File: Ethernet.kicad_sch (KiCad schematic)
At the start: 34 parts, among them J12 7499010211A, U12 LAN8742A, U13 USBLC6-4SC6, Y3 25Mhz

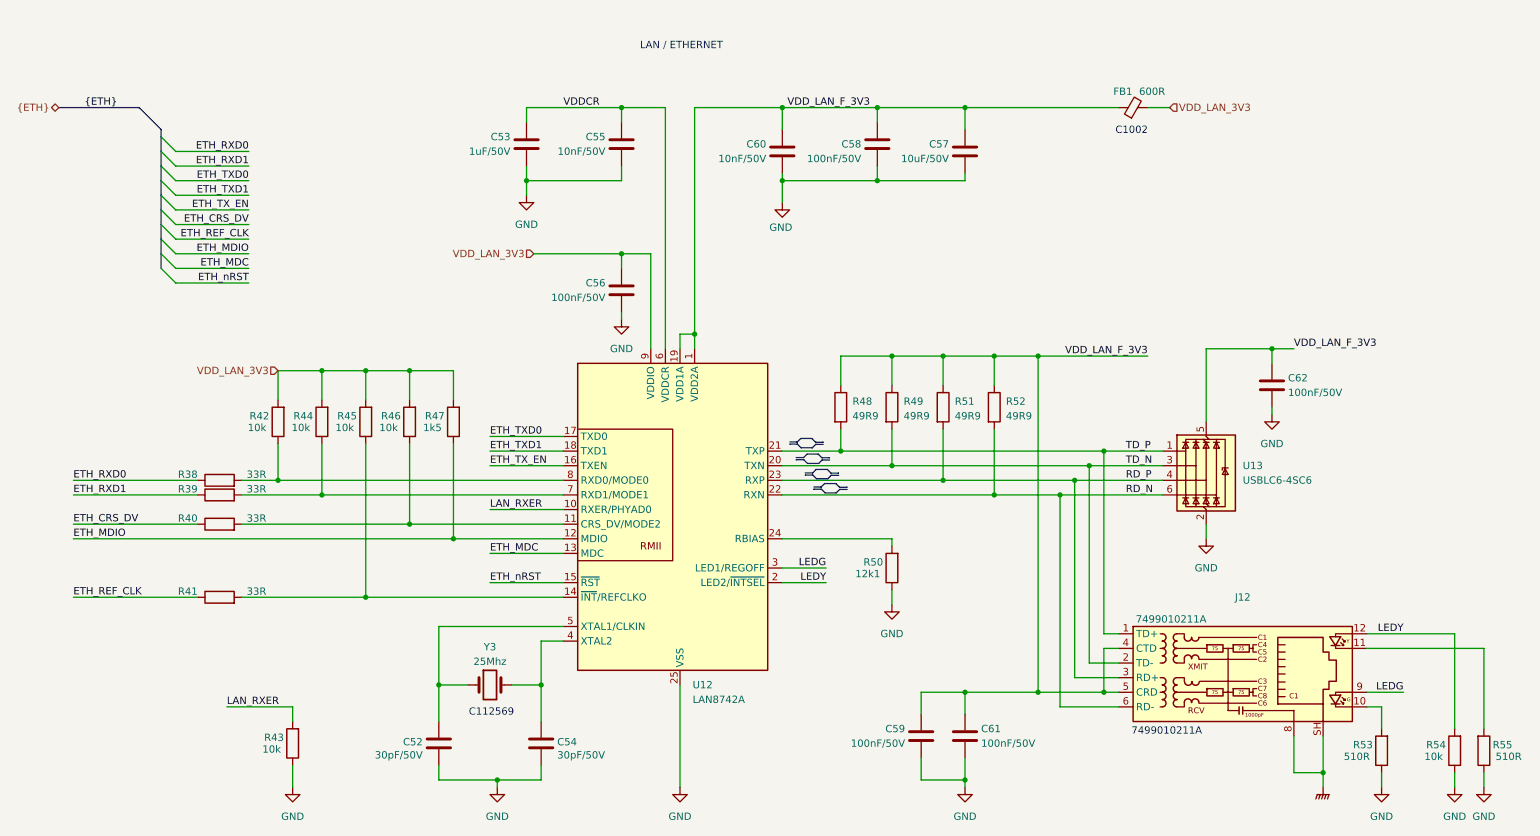
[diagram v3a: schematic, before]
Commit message: Se empieza a evaluar la conexión del ethernet con la carcasa, parte analog, dig y micro en posición, tambien se busca solución para la salida de led de las entradas digitales
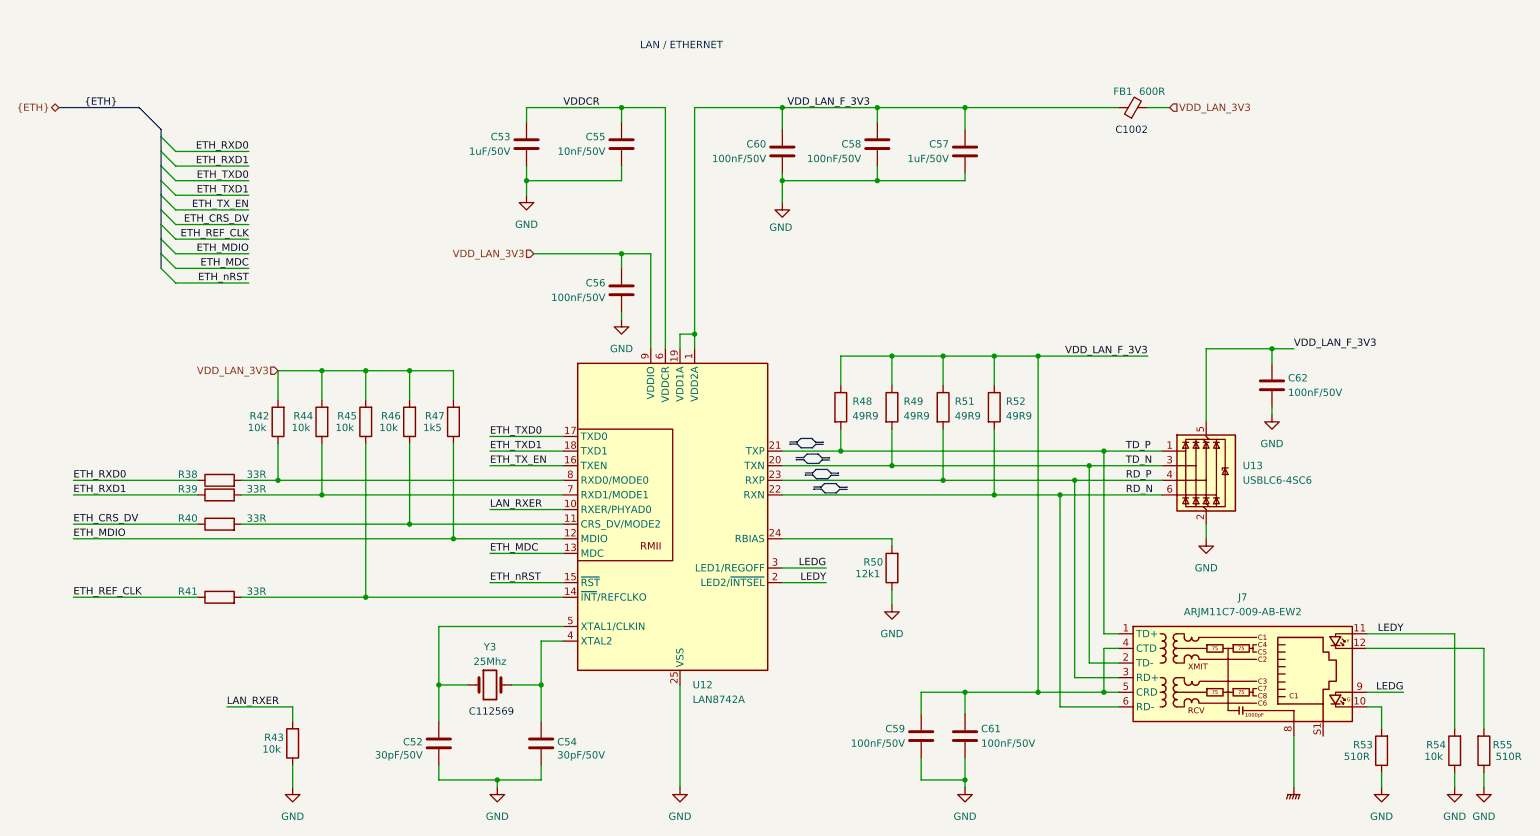
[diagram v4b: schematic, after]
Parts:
- removed J12: 7499010211A, Connector_RJ:RJ45_Wuerth_7499010211A_Horizontal, symbol Connector:RJ45_Wuerth_7499010211A
- added J7: ARJM11C7-009-AB-EW2, LIB_PCB_CONT:ARJM11C7-009-AB-EW2_Abracon, symbol LIB_SCH_CONTR:ARJM11C7-009-AB-EW2
- C57: value 10uF/50V -> 1uF/50V
- C60: value 10nF/50V -> 100nF/50V
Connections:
- net GNDPWR: now also J7.8
- net LEDG: now also J7.9
- net LEDY: now also J7.11
- net RD_N: now also J7.6 (RD-)
- net RD_P: now also J7.3 (RD+)
- net TD_N: now also J7.2 (TD-)
- net TD_P: now also J7.1 (TD+)
- net VDD_LAN_F_3V3: now also J7.4 (CTD), J7.5 (CRD)
- net at R53.2: now also J7.10
- net at R55.2: now also J7.12
- new net: J7.S1, J7.S2
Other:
- note removed: "7499010211A"
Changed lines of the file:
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@@
 		)
 	)
-	(text "7499010211A"
-		(exclude_from_sim no)
-		(at 221.742 140.208 0)
-		(effects
-			(font
-				(size 1.27 1.27)
-			)
-		)
-	)
 	(text "C1002"
 		(exclude_from_sim no)
@@
 	)
 	(junction
-		(at 248.92 147.32)
-		(diameter 0)
-		(color 0 0 0 0)
-	)
-	(junction
 		(at 97.79 106.68)
 		(diameter 0)
@@
 	(wire
 		(pts
-			(xy 248.92 140.97) (xy 248.92 147.32)
-		)
-		(stroke
-			(width 0)
-			(type default)
-		)
-	)
-	(wire
-		(pts
 			(xy 228.6 104.14) (xy 228.6 106.68)
 		)
@@
 		)
 	)
-	(wire
-		(pts
-			(xy 243.84 147.32) (xy 248.92 147.32)
-		)
-		(stroke
-			(width 0)
-			(type default)
-		)
-	)
 	(polyline
 		(pts
@@
 	(wire
 		(pts
-			(xy 248.92 147.32) (xy 248.92 149.86)
+			(xy 243.84 140.97) (xy 243.84 149.86)
 		)
 		(stroke
@@
 	(wire
 		(pts
-			(xy 243.84 140.97) (xy 243.84 147.32)
-		)
-		(stroke
-			(width 0)
-			(type default)
-		)
-	)
-	(wire
-		(pts
 			(xy 67.31 90.17) (xy 67.31 96.52)
 		)
@@
 			)
 		)
-		(property "Value" "10uF/50V"
+		(property "Value" "1uF/50V"
 			(at 183.896 40.64 0)
 			(effects
@@
 	(symbol
 		(lib_id "power:GNDPWR")
-		(at 248.92 149.86 0)
+		(at 243.84 149.86 0)
 		(unit 1)
 		(exclude_from_sim no)
@@
 		(dnp no)
 		(property "Reference" "#PWR051"
-			(at 248.92 154.94 0)
+			(at 243.84 154.94 0)
 			(effects
 				(font
@@
 		)
 		(property "Value" "GNDPWR"
-			(at 246.634 154.178 0)
+			(at 241.554 154.178 0)
 			(effects
 				(font
@@
 		)
 		(property "Footprint" ""
-			(at 248.92 151.13 0)
+			(at 243.84 151.13 0)
 			(effects
 				(font
@@
 		)
 		(property "Datasheet" ""
-			(at 248.92 151.13 0)
+			(at 243.84 151.13 0)
 			(effects
 				(font
@@
 		)
 		(property "Description" "Power symbol creates a global label with name \"GNDPWR\" , global ground"
-			(at 248.92 149.86 0)
+			(at 243.84 149.86 0)
 			(effects
 				(font
@@
 	)
 	(symbol
-		(lib_id "Connector:RJ45_Wuerth_7499010211A")
+		(lib_id "LIB_SCH_CONTR:ARJM11C7-009-AB-EW2")
 		(at 233.68 130.81 0)
 		(unit 1)
@@
 		(on_board yes)
 		(dnp no)
-		(property "Reference" "J12"
+		(fields_autoplaced yes)
+		(property "Reference" "J7"
 			(at 234.95 116.84 0)
 			(effects
@@
 			)
 		)
-		(property "Value" "7499010211A"
-			(at 222.504 120.65 0)
+		(property "Value" "ARJM11C7-009-AB-EW2"
+			(at 234.95 119.38 0)
 			(effects
 				(font
@@
 			)
 		)
-		(property "Footprint" "Connector_RJ:RJ45_Wuerth_7499010211A_Horizontal"
+		(property "Footprint" "LIB_PCB_CONT:ARJM11C7-009-AB-EW2_Abracon"
 			(at 233.68 118.11 0)
 			(effects
@@
 			)
 		)
-		(property "Datasheet" "https://www.we-online.com/components/products/datasheet/7499010211A.pdf"
+		(property "Datasheet" "https://abracon.com/Magnetics/ARJM11.pdf"
 			(at 233.68 114.3 0)
 			(effects
@@
 			)
 		)
-		(pin "12"
+		(pin "1"
 		)
-		(pin "7"
+		(pin "2"
 		)
-		(pin "SH"
+		(pin "11"
 		)
-		(pin "9"
+		(pin "S2"
 		)
-		(pin "3"
+		(pin "5"
 		)
-		(pin "10"
+		(pin "4"
 		)
-		(pin "2"
+		(pin "9"
 		)
-		(pin "1"
+		(pin "10"
 		)
 		(pin "8"
 		)
-		(pin "5"
-		)
-		(pin "11"
+		(pin "S1"
 		)
 		(pin "6"
 		)
-		(pin "4"
+		(pin "3"
+		)
+		(pin "7"
+		)
+		(pin "12"
 		)
 		(instances
 			(project ""
-				(path "/7cf65f8a-f9e1-4c97-ae3b-2bf5316c4d48/15cecee3-3ea4-4fda-9934-a7d023f81ee7"
-					(reference "J4")
-					(unit 1)
-				)
-			)
-			(project ""
 				(path "/af529cf8-e3d6-4568-89be-bc7010f8b835/8e0b582f-0020-4bc2-aca5-707ed1850aed"
-					(reference "J12")
+					(reference "J7")
 					(unit 1)
 				)
@@
 			)
 		)
-		(property "Value" "10nF/50V"
+		(property "Value" "100nF/50V"
 			(at 152.146 40.64 0)
 			(effects

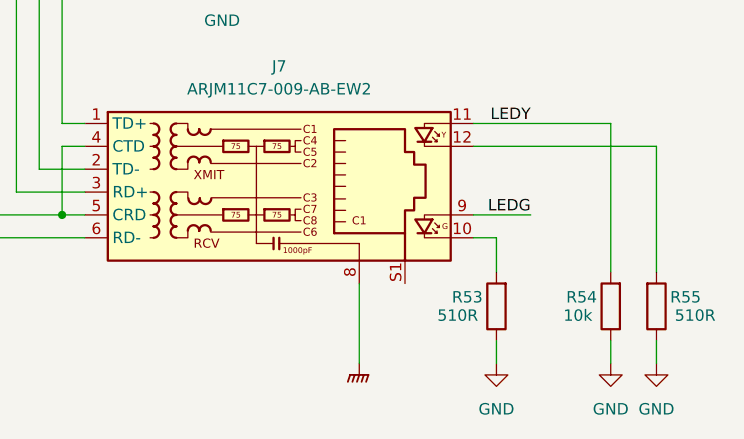
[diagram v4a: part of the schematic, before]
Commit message: Se traza vcc, digital, analog, relay, esta por terminar corregir GND y revisar nuevamente
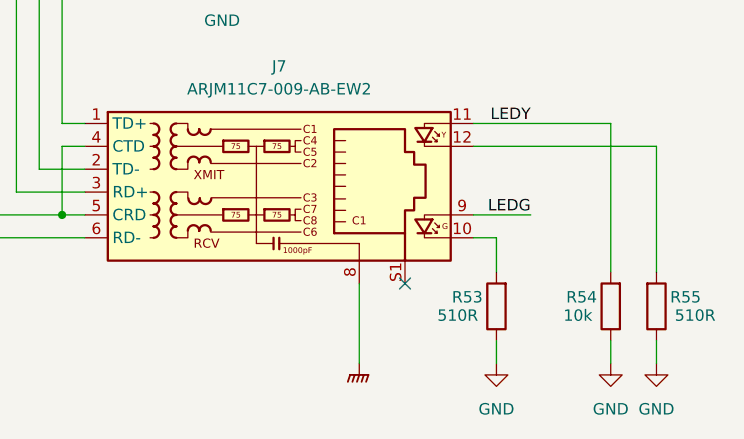
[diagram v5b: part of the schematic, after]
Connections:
- no-connect marks 0 -> 1
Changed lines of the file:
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@@
 		(color 0 0 0 0)
+	)
+	(no_connect
+		(at 248.92 140.97)
 	)
 	(bus_entry

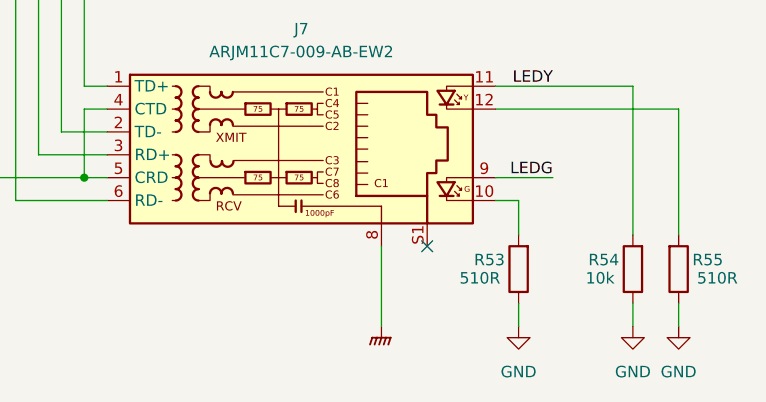
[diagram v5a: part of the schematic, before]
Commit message: Se termina de revisar la placa. Se corrige la terminación de los transformadores internos del puerto ethernet. Se revisa GND, espaciado, añadimos notas. Falta enlazar las partes de JLCPCN
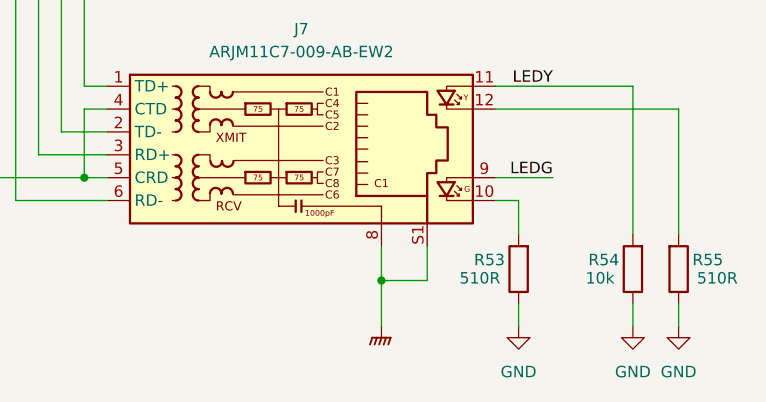
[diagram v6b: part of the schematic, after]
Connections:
- net GNDPWR: now also J7.S1, J7.S2
- no-connect marks 1 -> 0
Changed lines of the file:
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@@
+	)
+	(junction
+		(at 243.84 144.78)
+		(diameter 0)
+		(color 0 0 0 0)
 	)
 	(junction
@@
 		(color 0 0 0 0)
 	)
-	(no_connect
-		(at 248.92 140.97)
-	)
 	(bus_entry
 		(at 46.99 44.45)
@@
 	(wire
 		(pts
+			(xy 243.84 144.78) (xy 243.84 149.86)
+		)
+		(stroke
+			(width 0)
+			(type default)
+		)
+	)
+	(wire
+		(pts
 			(xy 154.94 44.45) (xy 154.94 48.26)
 		)
@@
 		)
 	)
+	(wire
+		(pts
+			(xy 248.92 140.97) (xy 248.92 144.78)
+		)
+		(stroke
+			(width 0)
+			(type default)
+		)
+	)
 	(polyline
 		(pts
@@
 	(wire
 		(pts
+			(xy 248.92 144.78) (xy 243.84 144.78)
+		)
+		(stroke
+			(width 0)
+			(type default)
+		)
+	)
+	(wire
+		(pts
 			(xy 137.16 71.12) (xy 137.16 73.66)
 		)
@@
 	(wire
 		(pts
-			(xy 243.84 140.97) (xy 243.84 149.86)
-		)
-		(stroke
+			(xy 243.84 140.97) (xy 243.84 144.78)
+		)
+		(stroke

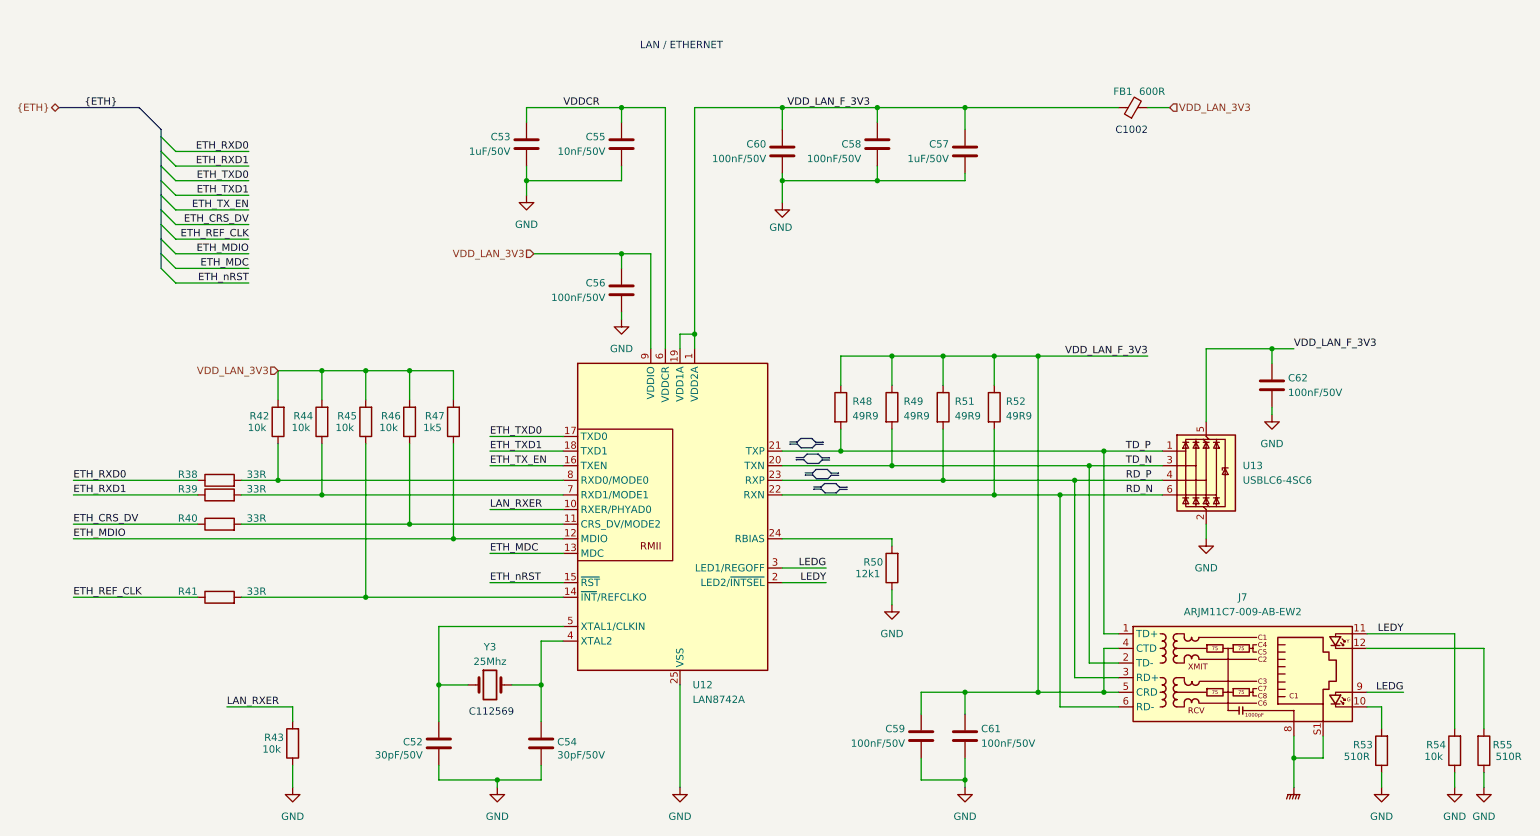
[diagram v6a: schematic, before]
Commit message: Se añaden leds a la entrada de los Namur. Se estandariza y revisan varios footprints de los capacitores. El cambio no fue demasiado, se corrigio en placa. Se hacen algunos cambios adicionales a los valores. Se realiza un avance para jlcpcb
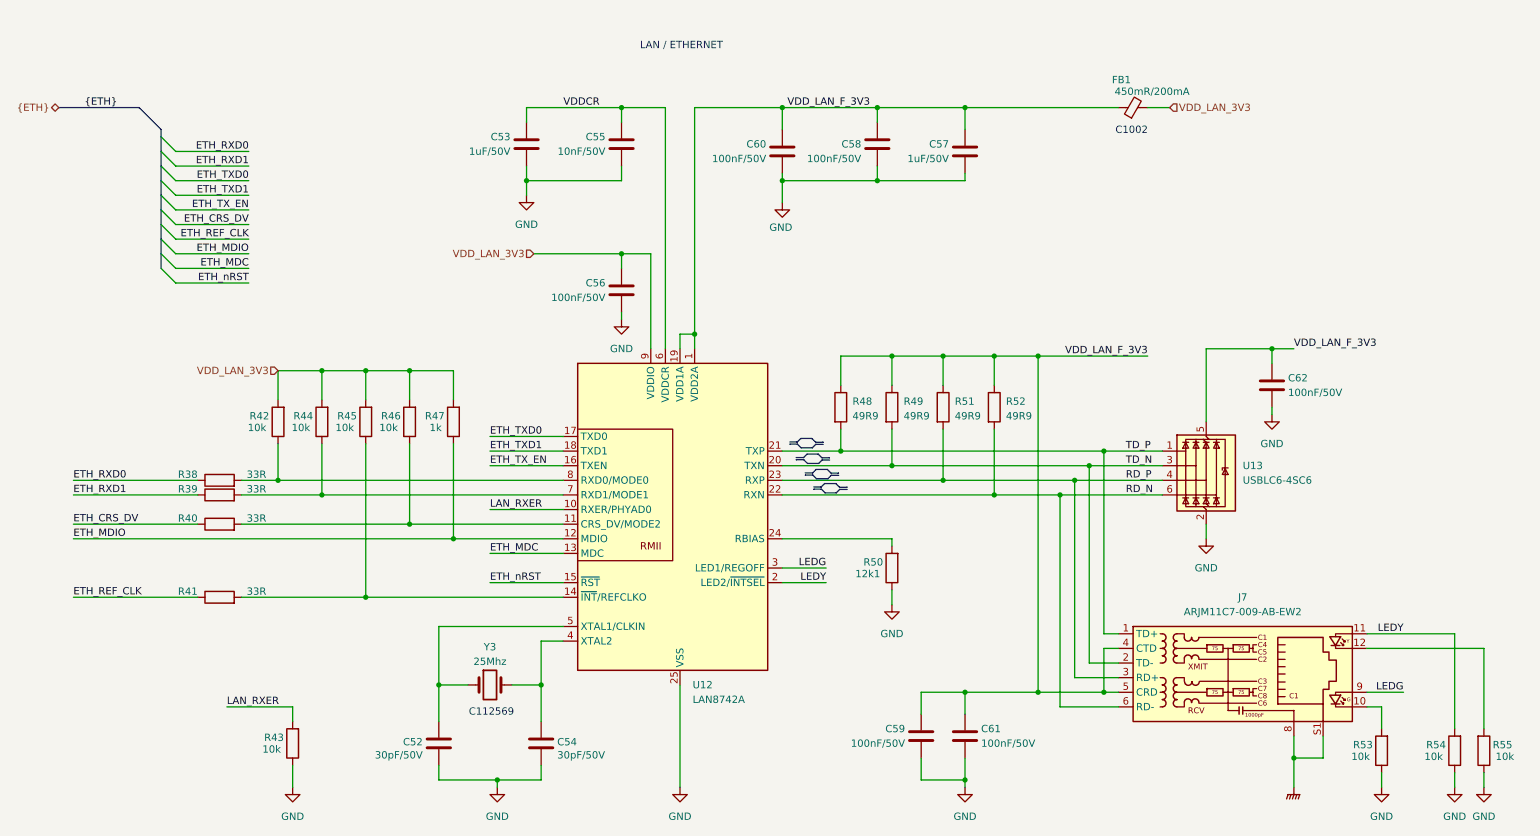
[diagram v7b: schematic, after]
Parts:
- C57: footprint Capacitor_SMD:C_0603_1608Metric -> Capacitor_SMD:C_0805_2012Metric
- FB1: value 600R -> 450mR/200mA; footprint Inductor_SMD:L_0805_2012Metric -> Inductor_SMD:L_0603_1608Metric
- R47: value 1k5 -> 1k
- R53, R55: value 510R -> 10k
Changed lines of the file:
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@@
 			)
 		)
-		(property "Value" "1k5"
+		(property "Value" "1k"
 			(at 95.758 87.376 0)
 			(effects
@@
 			)
 		)
-		(property "Value" "510R"
+		(property "Value" "10k"
 			(at 257.048 144.526 0)
 			(effects
@@
 			)
 		)
-		(property "Footprint" "Capacitor_SMD:C_0603_1608Metric"
+		(property "Footprint" "Capacitor_SMD:C_0805_2012Metric"
 			(at 185.7248 43.18 0)
 			(effects
@@
 		(dnp no)
 		(property "Reference" "FB1"
-			(at 214.122 28.956 90)
-			(effects
-				(font
-					(size 1.27 1.27)
-				)
-			)
-		)
-		(property "Value" "600R"
+			(at 213.868 26.924 90)
+			(effects
+				(font
+					(size 1.27 1.27)
+				)
+			)
+		)
+		(property "Value" "450mR/200mA"
 			(at 219.202 28.956 90)
 			(effects
@@
 			)
 		)
-		(property "Footprint" "Inductor_SMD:L_0805_2012Metric"
+		(property "Footprint" "Inductor_SMD:L_0603_1608Metric"
 			(at 215.9 33.528 90)
 			(effects
@@
 			)
 		)
-		(property "Value" "510R"
+		(property "Value" "10k"
 			(at 278.892 144.526 0)
 			(effects
